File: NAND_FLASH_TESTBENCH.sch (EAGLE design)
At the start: 11 parts, among them IC1 S35ML04G300WHI000

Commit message: fixed labels
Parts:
- JP1: device pinhead:PINHD-1X2/90 -> pinhead:PINHD-1X8
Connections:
- removed net 1: IC1.CS#, TP1.TP
- removed net 2: IC1.SO/IO1, TP2.TP
- removed net 3: IC1.WP#/IO2, TP3.TP
- removed net 5: IC1.SI/IO0, TP5.TP
- removed net 6: IC1.SCK, TP6.TP
- removed net 7: IC1.HOLD#/IO3, TP7.TP
- removed net V(IN): C1.1, IC1.VDD, JP1.1
- new net 3.3V: C1.1, IC1.VDD, JP1.8
- new net CS#: IC1.CS#, JP1.1, TP1.TP
- new net HOLD#/IO3: IC1.HOLD#/IO3, JP1.7, TP7.TP
- new net SCK: IC1.SCK, JP1.6, TP6.TP
- new net SI/IO0: IC1.SI/IO0, JP1.5, TP5.TP
- new net SO/IO1: IC1.SO/IO1, JP1.2, TP2.TP
- new net WP#/IO2: IC1.WP#/IO2, JP1.3, TP3.TP
- net GND: now also JP1.4; no longer JP1.2

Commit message: finished board layout
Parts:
- added TP10, TP11, TP12, TP13, TP14, TP9: (no value), SamacSys_Parts:S1751-46R
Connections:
- net 3.3V: now also TP8.TP
- net GND: now also TP10.TP, TP11.TP, TP12.TP, TP13.TP, TP14.TP, TP9.TP; no longer TP8.TP
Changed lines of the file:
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@@
 <part name="TP8" library="SamacSys_Parts" deviceset="S1751-46R" device=""/>
 <part name="JP1" library="pinhead" library_urn="urn:adsk.eagle:library:325" deviceset="PINHD-1X8" device="" package3d_urn="urn:adsk.eagle:package:22409/2"/>
+<part name="TP9" library="SamacSys_Parts" deviceset="S1751-46R" device=""/>
+<part name="TP10" library="SamacSys_Parts" deviceset="S1751-46R" device=""/>
+<part name="TP11" library="SamacSys_Parts" deviceset="S1751-46R" device=""/>
+<part name="TP12" library="SamacSys_Parts" deviceset="S1751-46R" device=""/>
+<part name="TP13" library="SamacSys_Parts" deviceset="S1751-46R" device=""/>
+<part name="TP14" library="SamacSys_Parts" deviceset="S1751-46R" device=""/>
 </parts>
 <sheets>
@@
 <attribute name="VALUE" x="-74.93" y="-22.86" size="1.778" layer="96"/>
 </instance>
+<instance part="TP9" gate="G$1" x="17.78" y="-40.64" smashed="yes">
+<attribute name="VALUE" x="12.7" y="-45.72" size="1.27" layer="96"/>
+<attribute name="NAME" x="12.7" y="-48.26" size="1.27" layer="95"/>
+</instance>
+<instance part="TP10" gate="G$1" x="35.56" y="-40.64" smashed="yes">
+<attribute name="VALUE" x="30.48" y="-45.72" size="1.27" layer="96"/>
+<attribute name="NAME" x="30.48" y="-48.26" size="1.27" layer="95"/>
+</instance>
+<instance part="TP11" gate="G$1" x="17.78" y="-60.96" smashed="yes">
+<attribute name="VALUE" x="12.7" y="-66.04" size="1.27" layer="96"/>
+<attribute name="NAME" x="12.7" y="-68.58" size="1.27" layer="95"/>
+</instance>
+<instance part="TP12" gate="G$1" x="35.56" y="-60.96" smashed="yes">
+<attribute name="VALUE" x="30.48" y="-66.04" size="1.27" layer="96"/>
+<attribute name="NAME" x="30.48" y="-68.58" size="1.27" layer="95"/>
+</instance>
+<instance part="TP13" gate="G$1" x="17.78" y="-81.28" smashed="yes">
+<attribute name="VALUE" x="12.7" y="-86.36" size="1.27" layer="96"/>
+</instance>
+<instance part="TP14" gate="G$1" x="35.56" y="-81.28" smashed="yes">
+<attribute name="VALUE" x="30.48" y="-86.36" size="1.27" layer="96"/>
+</instance>
 </instances>
 <busses>
@@
 </segment>
 <segment>
-<pinref part="TP8" gate="G$1" pin="TP"/>
-<wire x1="-5.08" y1="-93.98" x2="-5.08" y2="-91.44" width="0.1524" layer="91"/>
-<label x="-5.08" y="-91.44" size="1.778" layer="95"/>
-</segment>
-<segment>
 <pinref part="IC1" gate="G$1" pin="VSS"/>
 <wire x1="-12.7" y1="-15.24" x2="-17.78" y2="-15.24" width="0.1524" layer="91"/>
@@
 <wire x1="-71.12" y1="-7.62" x2="-63.5" y2="-7.62" width="0.1524" layer="91"/>
 <label x="-60.96" y="-7.62" size="1.778" layer="95"/>
+</segment>
+<segment>
+<pinref part="TP9" gate="G$1" pin="TP"/>
+<wire x1="17.78" y1="-33.02" x2="17.78" y2="-30.48" width="0.1524" layer="91"/>
+<label x="17.78" y="-30.48" size="1.778" layer="95"/>
+</segment>
+<segment>
+<pinref part="TP10" gate="G$1" pin="TP"/>
+<wire x1="35.56" y1="-33.02" x2="35.56" y2="-30.48" width="0.1524" layer="91"/>
+<label x="35.56" y="-30.48" size="1.778" layer="95"/>
+</segment>
+<segment>
+<pinref part="TP11" gate="G$1" pin="TP"/>
+<wire x1="17.78" y1="-53.34" x2="17.78" y2="-50.8" width="0.1524" layer="91"/>
+<label x="17.78" y="-50.8" size="1.778" layer="95"/>
+</segment>
+<segment>
+<pinref part="TP12" gate="G$1" pin="TP"/>
+<wire x1="35.56" y1="-53.34" x2="35.56" y2="-50.8" width="0.1524" layer="91"/>
+<label x="35.56" y="-50.8" size="1.778" layer="95"/>
+</segment>
+<segment>
+<pinref part="TP13" gate="G$1" pin="TP"/>
+<wire x1="17.78" y1="-73.66" x2="17.78" y2="-71.12" width="0.1524" layer="91"/>
+<label x="17.78" y="-71.12" size="1.778" layer="95"/>
+</segment>
+<segment>
+<pinref part="TP14" gate="G$1" pin="TP"/>
+<wire x1="35.56" y1="-73.66" x2="35.56" y2="-71.12" width="0.1524" layer="91"/>
+<label x="35.56" y="-71.12" size="1.778" layer="95"/>
 </segment>
 </net>
@@
 <label x="-60.96" y="-17.78" size="1.778" layer="95"/>
 </segment>
-</net>
+<segment>
+<pinref part="TP8" gate="G$1" pin="TP"/>
+<wire x1="-5.08" y1="-93.98" x2="-5.08" y2="-91.44" width="0.1524" layer="91"/>
+<label x="-5.08" y="-91.44" size="1.778" layer="95"/>
+</segment>
+</net>

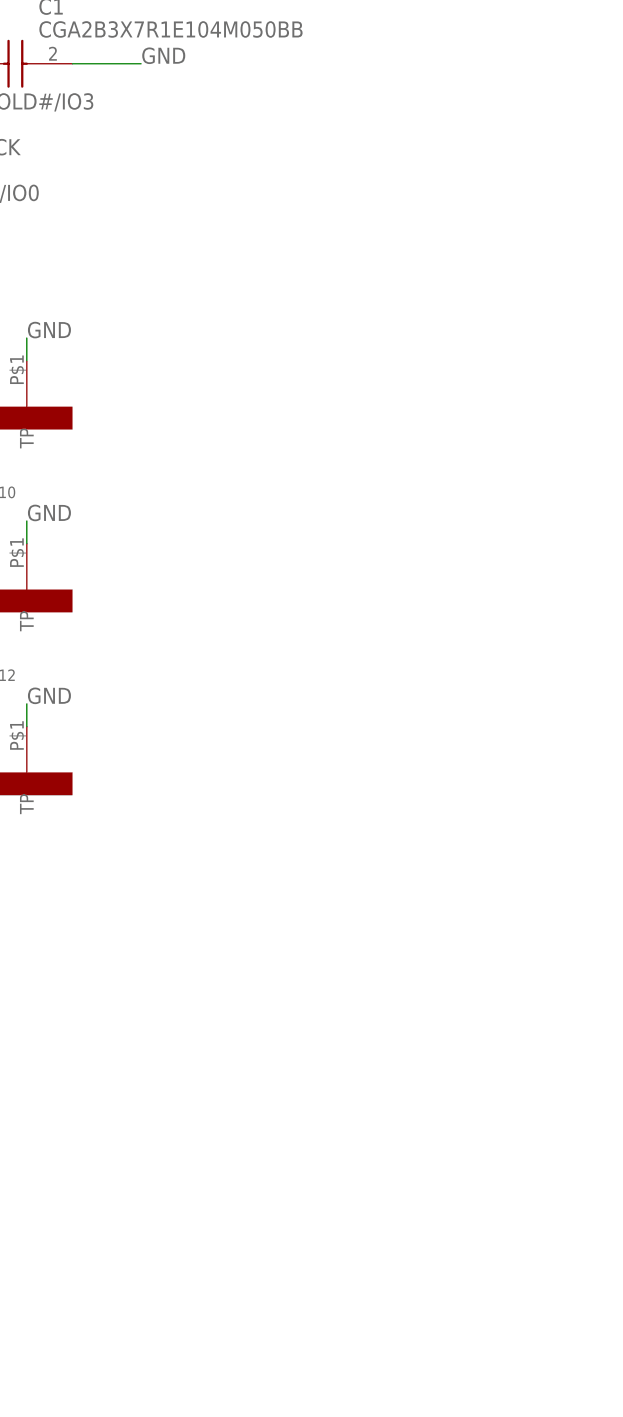
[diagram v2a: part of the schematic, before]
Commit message: updated layout
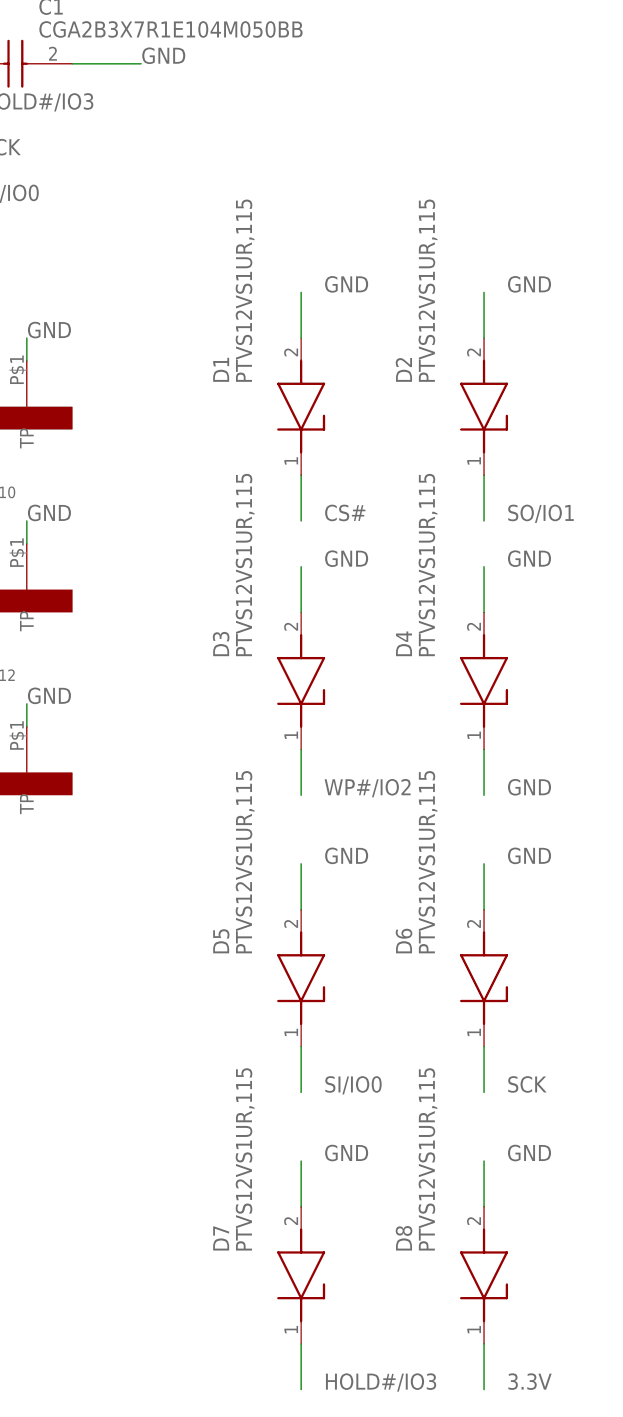
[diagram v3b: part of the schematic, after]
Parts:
- added D1, D2, D3, D4, D5, D6, D7, D8: PTVS12VS1UR,115, SamacSys_Parts:PTVS12VS1UR,115
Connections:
- net 3.3V: now also D8.K
- net CS#: now also D1.K
- net GND: now also D1.A, D2.A, D3.A, D4.A, D4.K, D5.A, D6.A, D7.A, D8.A
- net HOLD#/IO3: now also D7.K
- net SCK: now also D6.K
- net SI/IO0: now also D5.K
- net SO/IO1: now also D2.K
- net WP#/IO2: now also D3.K
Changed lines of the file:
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@@
 <part name="TP13" library="SamacSys_Parts" deviceset="S1751-46R" device=""/>
 <part name="TP14" library="SamacSys_Parts" deviceset="S1751-46R" device=""/>
+<part name="D1" library="SamacSys_Parts" deviceset="PTVS12VS1UR,115" device=""/>
+<part name="D2" library="SamacSys_Parts" deviceset="PTVS12VS1UR,115" device=""/>
+<part name="D3" library="SamacSys_Parts" deviceset="PTVS12VS1UR,115" device=""/>
+<part name="D4" library="SamacSys_Parts" deviceset="PTVS12VS1UR,115" device=""/>
+<part name="D5" library="SamacSys_Parts" deviceset="PTVS12VS1UR,115" device=""/>
+<part name="D6" library="SamacSys_Parts" deviceset="PTVS12VS1UR,115" device=""/>
+<part name="D7" library="SamacSys_Parts" deviceset="PTVS12VS1UR,115" device=""/>
+<part name="D8" library="SamacSys_Parts" deviceset="PTVS12VS1UR,115" device=""/>
 </parts>
 <sheets>
@@
 <attribute name="VALUE" x="30.48" y="-86.36" size="1.27" layer="96"/>
 </instance>
+<instance part="D1" gate="G$1" x="66.04" y="-45.72" smashed="yes" rot="R90">
+<attribute name="NAME" x="57.15" y="-35.56" size="1.778" layer="95" rot="R90" align="center-left"/>
+<attribute name="VALUE" x="59.69" y="-35.56" size="1.778" layer="96" rot="R90" align="center-left"/>
+</instance>
+<instance part="D2" gate="G$1" x="86.36" y="-45.72" smashed="yes" rot="R90">
+<attribute name="NAME" x="77.47" y="-35.56" size="1.778" layer="95" rot="R90" align="center-left"/>
+<attribute name="VALUE" x="80.01" y="-35.56" size="1.778" layer="96" rot="R90" align="center-left"/>
+</instance>
+<instance part="D3" gate="G$1" x="66.04" y="-76.2" smashed="yes" rot="R90">
+<attribute name="NAME" x="57.15" y="-66.04" size="1.778" layer="95" rot="R90" align="center-left"/>
+<attribute name="VALUE" x="59.69" y="-66.04" size="1.778" layer="96" rot="R90" align="center-left"/>
+</instance>
+<instance part="D4" gate="G$1" x="86.36" y="-76.2" smashed="yes" rot="R90">
+<attribute name="NAME" x="77.47" y="-66.04" size="1.778" layer="95" rot="R90" align="center-left"/>
+<attribute name="VALUE" x="80.01" y="-66.04" size="1.778" layer="96" rot="R90" align="center-left"/>
+</instance>
+<instance part="D5" gate="G$1" x="66.04" y="-109.22" smashed="yes" rot="R90">
+<attribute name="NAME" x="57.15" y="-99.06" size="1.778" layer="95" rot="R90" align="center-left"/>
+<attribute name="VALUE" x="59.69" y="-99.06" size="1.778" layer="96" rot="R90" align="center-left"/>
+</instance>
+<instance part="D6" gate="G$1" x="86.36" y="-109.22" smashed="yes" rot="R90">
+<attribute name="NAME" x="77.47" y="-99.06" size="1.778" layer="95" rot="R90" align="center-left"/>
+<attribute name="VALUE" x="80.01" y="-99.06" size="1.778" layer="96" rot="R90" align="center-left"/>
+</instance>
+<instance part="D7" gate="G$1" x="66.04" y="-142.24" smashed="yes" rot="R90">
+<attribute name="NAME" x="57.15" y="-132.08" size="1.778" layer="95" rot="R90" align="center-left"/>
+<attribute name="VALUE" x="59.69" y="-132.08" size="1.778" layer="96" rot="R90" align="center-left"/>
+</instance>
+<instance part="D8" gate="G$1" x="86.36" y="-142.24" smashed="yes" rot="R90">
+<attribute name="NAME" x="77.47" y="-132.08" size="1.778" layer="95" rot="R90" align="center-left"/>
+<attribute name="VALUE" x="80.01" y="-132.08" size="1.778" layer="96" rot="R90" align="center-left"/>
+</instance>
 </instances>
 <busses>
@@
 <label x="35.56" y="-71.12" size="1.778" layer="95"/>
 </segment>
+<segment>
+<pinref part="D1" gate="G$1" pin="A"/>
+<wire x1="66.04" y1="-30.48" x2="66.04" y2="-25.4" width="0.1524" layer="91"/>
+<label x="68.58" y="-25.4" size="1.778" layer="95"/>
+</segment>
+<segment>
+<pinref part="D2" gate="G$1" pin="A"/>
+<wire x1="86.36" y1="-30.48" x2="86.36" y2="-25.4" width="0.1524" layer="91"/>
+<label x="88.9" y="-25.4" size="1.778" layer="95"/>
+</segment>
+<segment>
+<pinref part="D3" gate="G$1" pin="A"/>
+<wire x1="66.04" y1="-60.96" x2="66.04" y2="-55.88" width="0.1524" layer="91"/>
+<label x="68.58" y="-55.88" size="1.778" layer="95"/>
+</segment>
+<segment>
+<pinref part="D4" gate="G$1" pin="A"/>
+<wire x1="86.36" y1="-60.96" x2="86.36" y2="-55.88" width="0.1524" layer="91"/>
+<label x="88.9" y="-55.88" size="1.778" layer="95"/>
+</segment>
+<segment>
+<pinref part="D5" gate="G$1" pin="A"/>
+<wire x1="66.04" y1="-93.98" x2="66.04" y2="-88.9" width="0.1524" layer="91"/>
+<label x="68.58" y="-88.9" size="1.778" layer="95"/>
+</segment>
+<segment>
+<pinref part="D6" gate="G$1" pin="A"/>
+<wire x1="86.36" y1="-93.98" x2="86.36" y2="-88.9" width="0.1524" layer="91"/>
+<label x="88.9" y="-88.9" size="1.778" layer="95"/>
+</segment>
+<segment>
+<pinref part="D7" gate="G$1" pin="A"/>
+<wire x1="66.04" y1="-127" x2="66.04" y2="-121.92" width="0.1524" layer="91"/>
+<label x="68.58" y="-121.92" size="1.778" layer="95"/>
+</segment>
+<segment>
+<pinref part="D8" gate="G$1" pin="A"/>
+<wire x1="86.36" y1="-127" x2="86.36" y2="-121.92" width="0.1524" layer="91"/>
+<label x="88.9" y="-121.92" size="1.778" layer="95"/>
+</segment>
+<segment>
+<pinref part="D4" gate="G$1" pin="K"/>
+<wire x1="86.36" y1="-76.2" x2="86.36" y2="-81.28" width="0.1524" layer="91"/>
+<label x="88.9" y="-81.28" size="1.778" layer="95"/>
+</segment>
 </net>
 <net name="CS#" class="0">
@@
 <label x="-60.96" y="0" size="1.778" layer="95"/>
 </segment>
+<segment>
+<pinref part="D1" gate="G$1" pin="K"/>
+<wire x1="66.04" y1="-45.72" x2="66.04" y2="-50.8" width="0.1524" layer="91"/>
+<label x="68.58" y="-50.8" size="1.778" layer="95"/>
+</segment>
 </net>
 <net name="SO/IO1" class="0">
@@
 <label x="-60.96" y="-2.54" size="1.778" layer="95"/>
 </segment>
+<segment>
+<pinref part="D2" gate="G$1" pin="K"/>
+<wire x1="86.36" y1="-45.72" x2="86.36" y2="-50.8" width="0.1524" layer="91"/>
+<label x="88.9" y="-50.8" size="1.778" layer="95"/>
+</segment>
 </net>
 <net name="WP#/IO2" class="0">
@@
 <label x="-60.96" y="-5.08" size="1.778" layer="95"/>
 </segment>
+<segment>
+<pinref part="D3" gate="G$1" pin="K"/>
+<wire x1="66.04" y1="-76.2" x2="66.04" y2="-81.28" width="0.1524" layer="91"/>
+<label x="68.58" y="-81.28" size="1.778" layer="95"/>
+</segment>
 </net>
 <net name="HOLD#/IO3" class="0">
@@
 <label x="-60.96" y="-15.24" size="1.778" layer="95"/>
 </segment>
+<segment>
+<pinref part="D7" gate="G$1" pin="K"/>
+<wire x1="66.04" y1="-142.24" x2="66.04" y2="-147.32" width="0.1524" layer="91"/>
+<label x="68.58" y="-147.32" size="1.778" layer="95"/>
+</segment>
 </net>
 <net name="SCK" class="0">
@@
 <label x="-60.96" y="-12.7" size="1.778" layer="95"/>
 </segment>
+<segment>
+<pinref part="D6" gate="G$1" pin="K"/>
+<wire x1="86.36" y1="-109.22" x2="86.36" y2="-114.3" width="0.1524" layer="91"/>
+<label x="88.9" y="-114.3" size="1.778" layer="95"/>
+</segment>
 </net>
 <net name="SI/IO0" class="0">
@@
 <wire x1="-71.12" y1="-10.16" x2="-63.5" y2="-10.16" width="0.1524" layer="91"/>
 <label x="-60.96" y="-10.16" size="1.778" layer="95"/>
+</segment>
+<segment>
+<pinref part="D5" gate="G$1" pin="K"/>
+<wire x1="66.04" y1="-109.22" x2="66.04" y2="-114.3" width="0.1524" layer="91"/>
+<label x="68.58" y="-114.3" size="1.778" layer="95"/>
 </segment>
 </net>
@@
 <label x="-5.08" y="-91.44" size="1.778" layer="95"/>
 </segment>
-</net>
+<segment>
+<pinref part="D8" gate="G$1" pin="K"/>
+<wire x1="86.36" y1="-142.24" x2="86.36" y2="-147.32" width="0.1524" layer="91"/>
+<label x="88.9" y="-147.32" size="1.778" layer="95"/>
+</segment>
+</net>
